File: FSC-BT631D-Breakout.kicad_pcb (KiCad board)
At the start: 2 copper layers, 46 parts, among them IC1 TLV320AIC3204IRHBR, J201 USB_C_Receptacle_USB2.0_16P, U202 AP63203WU-7

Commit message: power section done
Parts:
- added L201: 10uH, VLS5045EX-100M:VLS5045EX330M, F.Cu at (129.7, 59.2)
- added Q201: AONR21307, AONR21307:AONR21307, F.Cu at (128.6, 70.2)
- added U201: HUSB238_002DD, Package_DFN_QFN:DFN-10-1EP_3x3mm_P0.5mm_EP1.65x2.38mm_ThermalVias, F.Cu at (128.7, 65.6)
- moved C38 46.4 mm to (110.4, 56.4)
- moved C41 46.4 mm to (110.4, 63.9)
- moved C44 46.4 mm to (110.4, 68.9)
- moved C45 46.4 mm to (114.7, 56.4)
- moved R10 46.4 mm to (114.7, 68.9)
- moved R6 46.4 mm to (114.7, 63.9)
- moved C39 46.4 mm to (110.4, 58.9)
- moved C40 46.4 mm to (110.4, 61.4)
- moved C43 46.4 mm to (110.4, 66.4)
- moved C46 46.4 mm to (114.7, 58.9)
- moved R5 46.4 mm to (114.7, 61.4)
- moved R9 46.4 mm to (114.7, 66.4)
- moved R11 46.4 mm to (119.1, 56.4)
- moved R12 46.4 mm to (119.1, 58.9)
- moved R13 46.4 mm to (119.1, 61.4)
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
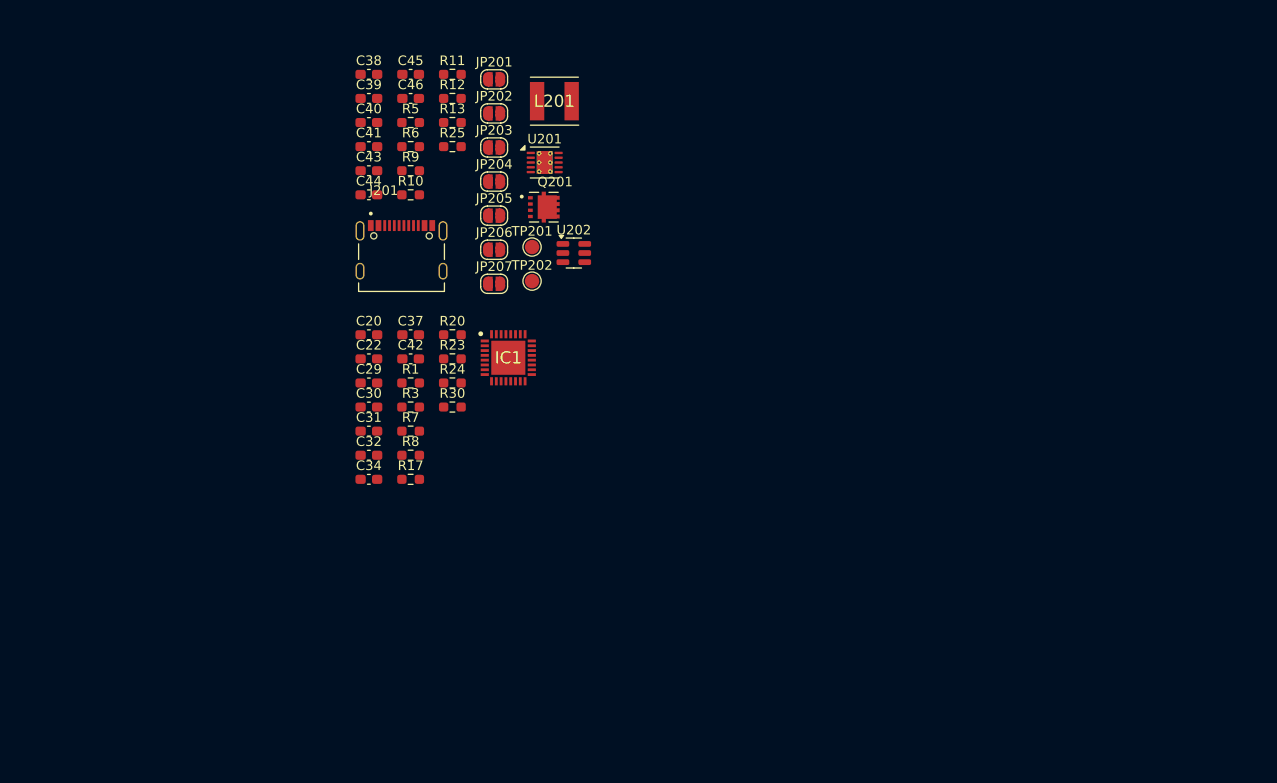
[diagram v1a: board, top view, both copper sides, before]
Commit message: schematic completed
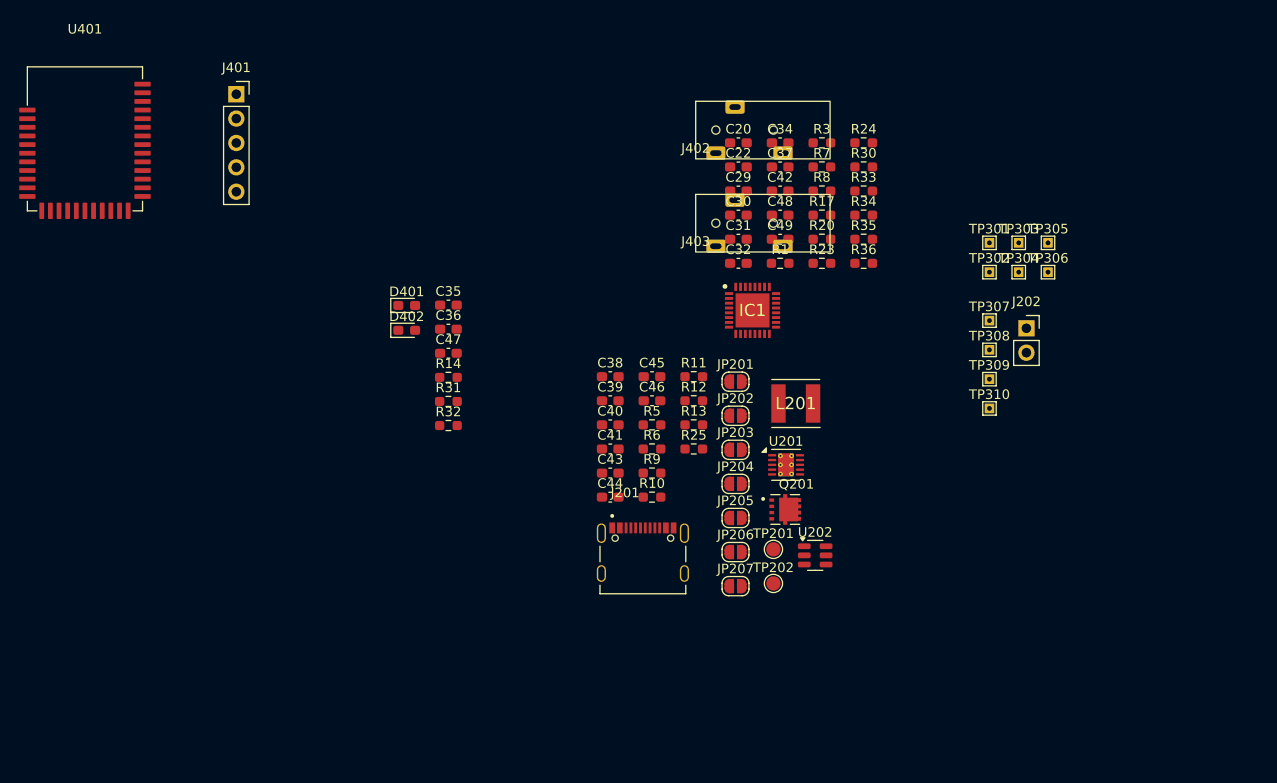
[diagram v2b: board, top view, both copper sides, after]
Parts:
- added C35: NC, Capacitor_SMD:C_0603_1608Metric_Pad1.08x0.95mm_HandSolder, F.Cu at (118.6, 80.4)
- added C36: NC, Capacitor_SMD:C_0603_1608Metric_Pad1.08x0.95mm_HandSolder, F.Cu at (118.6, 82.9)
- added C47: NC, Capacitor_SMD:C_0603_1608Metric_Pad1.08x0.95mm_HandSolder, F.Cu at (118.6, 85.4)
- added C48: 4.7uF, Capacitor_SMD:C_0603_1608Metric_Pad1.08x0.95mm_HandSolder, F.Cu at (153.2, 71.0)
- added C49: 4.7uF, Capacitor_SMD:C_0603_1608Metric_Pad1.08x0.95mm_HandSolder, F.Cu at (153.2, 73.6)
- added D401: LED2, LED_SMD:LED_0603_1608Metric_Pad1.05x0.95mm_HandSolder, F.Cu at (114.3, 80.5)
- added D402: LED1, LED_SMD:LED_0603_1608Metric_Pad1.05x0.95mm_HandSolder, F.Cu at (114.3, 83.0)
- added J202: J, Connector_PinSocket_2.54mm:PinSocket_1x02_P2.54mm_Vertical, F.Cu at (178.9, 82.8)
- added J401: UPDATE, Connector_PinSocket_2.54mm:PinSocket_1x05_P2.54mm_Vertical, F.Cu at (96.5, 58.5)
- added J402: LINE IN, XKB_PJ-3200:XKB_PJ-3200, F.Cu at (144.4, 64.6)
- added J403: LINE OUT, XKB_PJ-3200:XKB_PJ-3200, F.Cu at (144.4, 74.3)
- added R14: 0R, Resistor_SMD:R_0603_1608Metric_Pad0.98x0.95mm_HandSolder, F.Cu at (118.6, 87.9)
- added R31: 1K, Resistor_SMD:R_0603_1608Metric_Pad0.98x0.95mm_HandSolder, F.Cu at (118.6, 90.5)
- added R32: 1K, Resistor_SMD:R_0603_1608Metric_Pad0.98x0.95mm_HandSolder, F.Cu at (118.6, 93.0)
- added R33: 10K, Resistor_SMD:R_0603_1608Metric_Pad0.98x0.95mm_HandSolder, F.Cu at (161.9, 68.5)
- added R34: 10K, Resistor_SMD:R_0603_1608Metric_Pad0.98x0.95mm_HandSolder, F.Cu at (161.9, 71.0)
- added R35: 4.7K, Resistor_SMD:R_0603_1608Metric_Pad0.98x0.95mm_HandSolder, F.Cu at (161.9, 73.6)
- added R36: 4.7K, Resistor_SMD:R_0603_1608Metric_Pad0.98x0.95mm_HandSolder, F.Cu at (161.9, 76.1)
- added TP301: SCL, TestPoint:TestPoint_THTPad_1.0x1.0mm_Drill0.5mm, F.Cu at (175.0, 73.9)
- added TP302: SDA, TestPoint:TestPoint_THTPad_1.0x1.0mm_Drill0.5mm, F.Cu at (175.0, 77.0)
- added TP303: BLCK, TestPoint:TestPoint_THTPad_1.0x1.0mm_Drill0.5mm, F.Cu at (178.1, 73.9)
- added TP304: WS, TestPoint:TestPoint_THTPad_1.0x1.0mm_Drill0.5mm, F.Cu at (178.1, 77.0)
- added TP305: DOUT, TestPoint:TestPoint_THTPad_1.0x1.0mm_Drill0.5mm, F.Cu at (181.1, 73.9)
- added TP306: DIN, TestPoint:TestPoint_THTPad_1.0x1.0mm_Drill0.5mm, F.Cu at (181.1, 77.0)
- added TP307: VBUS, TestPoint:TestPoint_THTPad_1.0x1.0mm_Drill0.5mm, F.Cu at (175.0, 82.0)
- added TP308: VOUT, TestPoint:TestPoint_THTPad_1.0x1.0mm_Drill0.5mm, F.Cu at (175.0, 85.1)
- added TP309: 3.3V, TestPoint:TestPoint_THTPad_1.0x1.0mm_Drill0.5mm, F.Cu at (175.0, 88.1)
- added TP310: VDD, TestPoint:TestPoint_THTPad_1.0x1.0mm_Drill0.5mm, F.Cu at (175.0, 91.2)
- added U401: ~, FSC-BT631D:FSC-BT631D, F.Cu at (80.8, 63.1)
- moved C34 55.4 mm to (153.2, 63.5)
- moved R17 50.9 mm to (157.6, 71.0)
- moved R7 50.9 mm to (157.6, 66.0)
- moved R8 50.9 mm to (157.6, 68.5)
- moved R3 50.9 mm to (157.6, 63.5)
- moved R24 49.6 mm to (161.9, 63.5)
- moved R30 49.6 mm to (161.9, 66.0)
- moved C32 43.4 mm to (148.9, 76.1)
- moved C20 43.4 mm to (148.9, 63.5)
- moved C22 43.4 mm to (148.9, 66.0)
- moved C29 43.4 mm to (148.9, 68.5)
- moved C30 43.4 mm to (148.9, 71.0)
- moved C31 43.4 mm to (148.9, 73.6)
- moved C37 42.3 mm to (153.2, 66.0)
- moved C42 42.3 mm to (153.2, 68.5)
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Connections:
- net /power/VBUS renamed VBUS
- net Net-(IC1-AVDD) renamed /codec/AVDD

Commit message: FINALISED LAYOUT
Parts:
- removed C29, C30, C31: 10uF, Capacitor_SMD:C_0603_1608Metric_Pad1.08x0.95mm_HandSolder
- removed C32: 1uF, Capacitor_SMD:C_0603_1608Metric_Pad1.08x0.95mm_HandSolder
- removed C34: 220nF, Capacitor_SMD:C_0603_1608Metric_Pad1.08x0.95mm_HandSolder
- removed C35, C36, C47: NC, Capacitor_SMD:C_0603_1608Metric_Pad1.08x0.95mm_HandSolder
- removed C37, C39, C40, C41, C42, C43, C48, C49: 4.7uF, Capacitor_SMD:C_0603_1608Metric_Pad1.08x0.95mm_HandSolder
- removed C38: 1uF/50V, Capacitor_SMD:C_0603_1608Metric_Pad1.08x0.95mm_HandSolder
- removed C44: 0.1uF, Capacitor_SMD:C_0603_1608Metric_Pad1.08x0.95mm_HandSolder
- removed C45, C46: 22uF, Capacitor_SMD:C_0603_1608Metric_Pad1.08x0.95mm_HandSolder
- removed D401: LED2, LED_SMD:LED_0603_1608Metric_Pad1.05x0.95mm_HandSolder
- removed D402: LED1, LED_SMD:LED_0603_1608Metric_Pad1.05x0.95mm_HandSolder
- removed J201: USB_C_Receptacle_USB2.0_16P, SHOUHAN_TYPE-C_16PIN_2MD__073:SHOUHAN_TYPE-C_16PIN_2MD__073
- removed J202: J, Connector_PinSocket_2.54mm:PinSocket_1x02_P2.54mm_Vertical
- removed J401: UPDATE, Connector_PinSocket_2.54mm:PinSocket_1x05_P2.54mm_Vertical
- removed J402: LINE IN, XKB_PJ-3200:XKB_PJ-3200
- removed J403: LINE OUT, XKB_PJ-3200:XKB_PJ-3200
- removed JP201: 5V, Jumper:SolderJumper-2_P1.3mm_Open_RoundedPad1.0x1.5mm
- removed JP202: 9V, Jumper:SolderJumper-2_P1.3mm_Open_RoundedPad1.0x1.5mm
- removed JP203: 12V, Jumper:SolderJumper-2_P1.3mm_Open_RoundedPad1.0x1.5mm
- removed JP204: 15V, Jumper:SolderJumper-2_P1.3mm_Open_RoundedPad1.0x1.5mm
- removed JP205: 18V, Jumper:SolderJumper-2_P1.3mm_Open_RoundedPad1.0x1.5mm
- removed JP206: 1.25A, Jumper:SolderJumper-2_P1.3mm_Open_RoundedPad1.0x1.5mm
- removed JP207: 2.25A, Jumper:SolderJumper-2_P1.3mm_Open_RoundedPad1.0x1.5mm
- removed L201: 10uH, VLS5045EX-100M:VLS5045EX330M
- removed Q201: AONR21307, AONR21307:AONR21307
- removed R30, R35, R36: 4.7K, Resistor_SMD:R_0603_1608Metric_Pad0.98x0.95mm_HandSolder
- removed R31, R32: 1K, Resistor_SMD:R_0603_1608Metric_Pad0.98x0.95mm_HandSolder
- removed R33, R34: 10K, Resistor_SMD:R_0603_1608Metric_Pad0.98x0.95mm_HandSolder
- removed TP201: SCL, TestPoint:TestPoint_Pad_D1.5mm
- removed TP202: SDA, TestPoint:TestPoint_Pad_D1.5mm
- removed TP301: SCL, TestPoint:TestPoint_THTPad_1.0x1.0mm_Drill0.5mm
- removed TP302: SDA, TestPoint:TestPoint_THTPad_1.0x1.0mm_Drill0.5mm
- removed TP303: BLCK, TestPoint:TestPoint_THTPad_1.0x1.0mm_Drill0.5mm
- removed TP304: WS, TestPoint:TestPoint_THTPad_1.0x1.0mm_Drill0.5mm
- removed TP305: DOUT, TestPoint:TestPoint_THTPad_1.0x1.0mm_Drill0.5mm
- removed TP306: DIN, TestPoint:TestPoint_THTPad_1.0x1.0mm_Drill0.5mm
- removed TP307: VBUS, TestPoint:TestPoint_THTPad_1.0x1.0mm_Drill0.5mm
- removed TP308: VOUT, TestPoint:TestPoint_THTPad_1.0x1.0mm_Drill0.5mm
- removed TP309: 3.3V, TestPoint:TestPoint_THTPad_1.0x1.0mm_Drill0.5mm
- removed TP310: VDD, TestPoint:TestPoint_THTPad_1.0x1.0mm_Drill0.5mm
- removed U201: HUSB238_002DD, Package_DFN_QFN:DFN-10-1EP_3x3mm_P0.5mm_EP1.65x2.38mm_ThermalVias
- removed U202: AP63203WU-7, Package_TO_SOT_SMD:TSOT-23-6
- removed U401: ~, FSC-BT631D:FSC-BT631D
- added C1: 4.7uF, Capacitor_SMD:C_0603_1608Metric_Pad1.08x0.95mm_HandSolder, F.Cu at (116.8, 105.4)
- added C10: 10uF, Capacitor_SMD:C_0603_1608Metric_Pad1.08x0.95mm_HandSolder, F.Cu at (153.7, 100.3)
- added C11: 4.7uF, Capacitor_SMD:C_0603_1608Metric_Pad1.08x0.95mm_HandSolder, F.Cu at (153.7, 97.8)
- added C12: 1uF, Capacitor_SMD:C_0603_1608Metric_Pad1.08x0.95mm_HandSolder, F.Cu at (153.7, 102.9)
- added C13: 220nF, Capacitor_SMD:C_0603_1608Metric_Pad1.08x0.95mm_HandSolder, F.Cu at (153.7, 92.7)
- added C14: 100nF, Capacitor_SMD:C_0603_1608Metric_Pad1.08x0.95mm_HandSolder, F.Cu at (153.7, 105.4)
- added C15: 4.7uF, Capacitor_SMD:C_0603_1608Metric_Pad1.08x0.95mm_HandSolder, F.Cu at (149.9, 105.4)
- added C16: 4.7uF, Capacitor_SMD:C_0603_1608Metric_Pad1.08x0.95mm_HandSolder, F.Cu at (135.9, 105.4)
- added C17: 4.7uF, Capacitor_SMD:C_0603_1608Metric_Pad1.08x0.95mm_HandSolder, F.Cu at (141.0, 105.4)
- added C18: 10uF, Capacitor_SMD:C_0603_1608Metric_Pad1.08x0.95mm_HandSolder, F.Cu at (144.8, 105.4)
- added C19: 4.7uF, Capacitor_SMD:C_0603_1608Metric_Pad1.08x0.95mm_HandSolder, F.Cu at (147.3, 105.4)
- added C2: 4.7uF, Capacitor_SMD:C_0603_1608Metric_Pad1.08x0.95mm_HandSolder, F.Cu at (116.8, 102.9)
- added C21: NC, Capacitor_SMD:C_0603_1608Metric_Pad1.08x0.95mm_HandSolder, F.Cu at (130.7, 58.9)
- added C3: 4.7uF, Capacitor_SMD:C_0603_1608Metric_Pad1.08x0.95mm_HandSolder, F.Cu at (116.8, 100.3)
- added C4: 1uF/50V, Capacitor_SMD:C_0603_1608Metric_Pad1.08x0.95mm_HandSolder, F.Cu at (106.7, 110.5)
- added C5: 0.1uF, Capacitor_SMD:C_0603_1608Metric_Pad1.08x0.95mm_HandSolder, F.Cu at (104.1, 95.2)
- added C6: 4.7uF, Capacitor_SMD:C_0603_1608Metric_Pad1.08x0.95mm_HandSolder, F.Cu at (111.7, 96.5)
- added C7: 22uF, Capacitor_SMD:C_0603_1608Metric_Pad1.08x0.95mm_HandSolder, F.Cu at (113.0, 91.4)
- added C8: 22uF, Capacitor_SMD:C_0603_1608Metric_Pad1.08x0.95mm_HandSolder, F.Cu at (115.5, 91.4)
- added C9: 10uF, Capacitor_SMD:C_0603_1608Metric_Pad1.08x0.95mm_HandSolder, F.Cu at (153.7, 95.2)
- added D1: 3.3V, LED_SMD:LED_0603_1608Metric_Pad1.05x0.95mm_HandSolder, F.Cu at (100.3, 86.4)
- added D2: VDD, LED_SMD:LED_0603_1608Metric_Pad1.05x0.95mm_HandSolder, F.Cu at (115.5, 86.4)
- added D3: LED1, LED_SMD:LED_0603_1608Metric_Pad1.05x0.95mm_HandSolder, F.Cu at (120.0, 82.0)
- added D4: LED2, LED_SMD:LED_0603_1608Metric_Pad1.05x0.95mm_HandSolder, F.Cu at (124.5, 82.0)
- added J1: USB_C_Receptacle_USB2.0_16P, SHOUHAN_TYPE-C_16PIN_2MD__073:SHOUHAN_TYPE-C_16PIN_2MD__073, F.Cu at (104.1, 123.2)
- added J10: PIO, Connector_PinSocket_2.54mm:PinSocket_1x08_P2.54mm_Vertical, F.Cu at (94.0, 66.0)
- added J2: J, Connector_PinSocket_2.54mm:PinSocket_1x02_P2.54mm_Vertical, F.Cu at (106.7, 81.3)
- added J3: LINE IN, XKB_PJ-3200:XKB_PJ-3200, F.Cu at (140.8, 126.3)
- added J4: LINE OUT, XKB_PJ-3200:XKB_PJ-3200, F.Cu at (154.8, 126.3)
- added J5: USB_B_Micro, KH-MICRO5P-JN:KH-MICRO5P-JN, F.Cu at (157.5, 86.4)
- added J6: UPDATE, Connector_PinSocket_2.54mm:PinSocket_1x05_P2.54mm_Vertical, F.Cu at (160.0, 61.0)
- added J7: UART, Connector_PinSocket_2.54mm:PinSocket_1x06_P2.54mm_Vertical, F.Cu at (140.7, 55.9)
- added J8: I2C, Connector_PinSocket_2.54mm:PinSocket_1x04_P2.54mm_Vertical, F.Cu at (94.0, 88.9)
- added J9: NFC, Connector_PinSocket_2.54mm:PinSocket_1x02_P2.54mm_Vertical, F.Cu at (111.3, 75.7)
- added JP1: 5V, Jumper:SolderJumper-2_P1.3mm_Open_RoundedPad1.0x1.5mm, F.Cu at (99.0, 110.5)
- added JP2: 9V, Jumper:SolderJumper-2_P1.3mm_Open_RoundedPad1.0x1.5mm, F.Cu at (99.0, 108.0)
- added JP3: 12V, Jumper:SolderJumper-2_P1.3mm_Open_RoundedPad1.0x1.5mm, F.Cu at (99.0, 105.4)
- added JP4: 15V, Jumper:SolderJumper-2_P1.3mm_Open_RoundedPad1.0x1.5mm, F.Cu at (99.0, 102.9)
- added JP5: 1.25A, Jumper:SolderJumper-2_P1.3mm_Open_RoundedPad1.0x1.5mm, F.Cu at (119.4, 113.0)
- added JP6: 18V, Jumper:SolderJumper-2_P1.3mm_Open_RoundedPad1.0x1.5mm, F.Cu at (99.0, 100.3)
- added JP7: 2.25A, Jumper:SolderJumper-2_P1.3mm_Open_RoundedPad1.0x1.5mm, F.Cu at (119.4, 108.0)
- added JP8: LED1_S, Jumper:SolderJumper-2_P1.3mm_Bridged2Bar_RoundedPad1.0x1.5mm, F.Cu at (120.0, 75.7)
- added JP9: LED2_S, Jumper:SolderJumper-2_P1.3mm_Bridged2Bar_RoundedPad1.0x1.5mm, F.Cu at (124.5, 75.7)
- added L1: 10uH, VLS5045EX-100M:VLS5045EX330M, F.Cu at (107.9, 88.9)
- added Q1: AONR21307, AONR21307:AONR21307, F.Cu at (111.7, 105.4)
- added R15: 4.7K, Resistor_SMD:R_0603_1608Metric_Pad0.98x0.95mm_HandSolder, F.Cu at (135.9, 108.0)
- added R16: 0R, Resistor_SMD:R_0603_1608Metric_Pad0.98x0.95mm_HandSolder, F.Cu at (142.2, 92.7)
- added R18: 10K, Resistor_SMD:R_0603_1608Metric_Pad0.98x0.95mm_HandSolder, F.Cu at (141.0, 110.5)
- added R19: 4.7K, Resistor_SMD:R_0603_1608Metric_Pad0.98x0.95mm_HandSolder, F.Cu at (141.0, 108.0)
- added R2: 10R, Resistor_SMD:R_0603_1608Metric_Pad0.98x0.95mm_HandSolder, F.Cu at (106.7, 113.0)
- added R21: 4.7K, Resistor_SMD:R_0603_1608Metric_Pad0.98x0.95mm_HandSolder, F.Cu at (135.9, 97.8)
- added R22: 33R, Resistor_SMD:R_0603_1608Metric_Pad0.98x0.95mm_HandSolder, F.Cu at (135.9, 95.2)
- added R26: 0R, Resistor_SMD:R_0603_1608Metric_Pad0.98x0.95mm_HandSolder, F.Cu at (105.2, 65.0)
- added R27: 1K, Resistor_SMD:R_0603_1608Metric_Pad0.98x0.95mm_HandSolder, F.Cu at (120.0, 79.5)
- added R28: 1K, Resistor_SMD:R_0603_1608Metric_Pad0.98x0.95mm_HandSolder, F.Cu at (124.5, 79.5)
- added R4: 6K, Resistor_SMD:R_0603_1608Metric_Pad0.98x0.95mm_HandSolder, F.Cu at (104.1, 108.0)
- added TP1: VBUS, TestPoint:TestPoint_THTPad_1.0x1.0mm_Drill0.5mm, F.Cu at (99.0, 115.6)
- added TP10: LOR, TestPoint:TestPoint_THTPad_1.0x1.0mm_Drill0.5mm, F.Cu at (146.8, 115.3)
- added TP11: DIN, TestPoint:TestPoint_THTPad_1.0x1.0mm_Drill0.5mm, F.Cu at (139.7, 86.4)
- added TP12: LOL, TestPoint:TestPoint_THTPad_1.0x1.0mm_Drill0.5mm, F.Cu at (143.8, 115.3)
- added TP13: SCL, TestPoint:TestPoint_THTPad_1.0x1.0mm_Drill0.5mm, F.Cu at (129.5, 95.2)
- added TP14: SDA, TestPoint:TestPoint_THTPad_1.0x1.0mm_Drill0.5mm, F.Cu at (129.5, 100.3)
- added TP2: SCL, TestPoint:TestPoint_Pad_D1.5mm, F.Cu at (115.5, 115.6)
- added TP3: SDA, TestPoint:TestPoint_Pad_D1.5mm, F.Cu at (111.7, 115.6)
- added TP4: VOUT, TestPoint:TestPoint_THTPad_1.0x1.0mm_Drill0.5mm, F.Cu at (115.5, 96.5)
- added TP5: 3.3V, TestPoint:TestPoint_THTPad_1.0x1.0mm_Drill0.5mm, F.Cu at (102.8, 81.3)
- added TP6: VDD, TestPoint:TestPoint_THTPad_1.0x1.0mm_Drill0.5mm, F.Cu at (113.0, 81.3)
- added TP7: BLCK, TestPoint:TestPoint_THTPad_1.0x1.0mm_Drill0.5mm, F.Cu at (147.3, 86.4)
- added TP8: WS, TestPoint:TestPoint_THTPad_1.0x1.0mm_Drill0.5mm, F.Cu at (144.8, 86.4)
- added TP9: DOUT, TestPoint:TestPoint_THTPad_1.0x1.0mm_Drill0.5mm, F.Cu at (142.2, 86.4)
- added U1: HUSB238_002DD, Package_DFN_QFN:DFN-10-1EP_3x3mm_P0.5mm_EP1.65x2.38mm_ThermalVias, F.Cu at (111.7, 110.5)
- added U2: AP63203WU-7, Package_TO_SOT_SMD:TSOT-23-6, F.Cu at (107.9, 96.5)
- added U3: ~, FSC-BT631D:FSC-BT631D, F.Cu at (116.8, 61.0)
- C20: value 100nF -> NC
- C22: value 4.7uF -> NC
- R1: value 0R -> 49.9K
- R10: value 10K -> 1K
- R11: value 14K -> 220K
- R12: value 18K -> 0R
- R13: value 14K -> 0R
- R14: value 0R -> 10K
- R17: value 4.7K -> 0R
- R20: value 220K -> 4.7K
- R24: value 33R -> 22R
- R25: value 10R -> 22R
- R3: value 0R -> 5.1K
- R5: value 49.9K -> 10K
- R6: value 5.1K -> 14K
- R7: value 0R -> 18K
- R8: value 0R -> 14K
- R9: value 6K -> 1K
- moved R3 72.8 mm to (106.7, 115.6), turned to 180 degrees
- moved R1 64.6 mm to (102.1, 115.6), turned to 180 degrees
- moved R7 63.5 mm to (104.1, 100.3), turned to 180 degrees
- moved R8 56.7 mm to (119.4, 110.5), turned to 180 degrees
- moved R9 42.9 mm to (100.3, 81.3), turned to 90 degrees
- moved R5 37.9 mm to (104.1, 105.4), turned to 180 degrees
- moved R6 36.5 mm to (104.1, 102.9), turned to 180 degrees
- moved R20 36.4 mm to (135.9, 102.9)
- moved R23 32.5 mm to (135.9, 100.3)
- moved R10 30.9 mm to (115.5, 81.3), turned to 90 degrees
- moved R14 28.4 mm to (135.9, 110.5), turned to 180 degrees
- moved R17 28.1 mm to (139.7, 92.7), turned to -90 degrees
- moved R24 21.9 mm to (153.8, 83.9), turned to 90 degrees
- moved C20 19.5 mm to (130.7, 56.4)
- moved C22 18.7 mm to (130.7, 61.5)
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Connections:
- C20 pad 1: +3V3 -> Net-(U3-RF)
- C20 pad 2: GND -> Net-(AE1-A)
- C22 pad 1: /codec/AVDD -> GND
- C22 pad 2: GND -> Net-(AE1-A)
- IC1 pad 15: L_LIN2 -> L_LINE2
- IC1 pad 22: unconnected-(IC1-LOL-Pad22) -> Net-(IC1-LOL)
- IC1 pad 23: unconnected-(IC1-LOR-Pad23) -> Net-(IC1-LOR)
- IC1 pad 26: +3V3 -> +3.3V
- IC1 pad 30: +3V3 -> +3.3V
- IC1 pad 6: +3V3 -> +3.3V
- R1 pad 1: P0.15/I2S_DOUT -> Net-(Q1-Pad4)
- R1 pad 2: /codec/I2S2_DO -> VBUS
- R10 pad 1: /power/VSET -> Net-(D2-A)
- R10 pad 2: Net-(JP203-A) -> VDD
- R11 pad 1: /power/VSET -> Net-(IC1-~{RESET})
- R11 pad 2: Net-(JP204-A) -> +3.3V
- R12 pad 1: /power/VSET -> P0.14/I2S_BCLK
- R12 pad 2: Net-(JP205-A) -> /codec/I2S2_CLK
- R13 pad 1: /power/ISET -> P0.16/I2S_WS
- R13 pad 2: Net-(JP207-A) -> /codec/I2S2_WS
- R14 pad 1: VDD -> Net-(C16-Pad1)
- R17 pad 1: +3V3 -> P0.13/I2S_DIN
- R17 pad 2: Net-(IC1-SCL/~{SS}) -> /codec/I2S2_DI
- R20 pad 1: Net-(IC1-~{RESET}) -> +3.3V
- R20 pad 2: +3V3 -> Net-(IC1-SDA/MOSI)
- R23 pad 1: P1.03/I2C_SCL -> P1.02/I2C_SDA
- R23 pad 2: Net-(IC1-SCL/~{SS}) -> Net-(IC1-SDA/MOSI)
- R24 pad 1: P1.02/I2C_SDA -> /module/MOD_D+
- R24 pad 2: Net-(IC1-SDA/MOSI) -> /module/USB_D+
- R25 pad 1: Net-(U201-VIN) -> /module/MOD_D-
- R25 pad 2: VBUS -> /module/USB_D-
- R3 pad 1: P0.14/I2S_BCLK -> Net-(U1-GATE)
- R3 pad 2: /codec/I2S2_CLK -> Net-(Q1-Pad4)
- R5 pad 1: Net-(Q201-Pad4) -> /power/VSET
- R5 pad 2: VBUS -> Net-(JP3-A)
- R6 pad 1: Net-(U201-GATE) -> /power/VSET
- R6 pad 2: Net-(Q201-Pad4) -> Net-(JP4-A)
- R7 pad 1: P0.13/I2S_DIN -> /power/VSET
- R7 pad 2: /codec/I2S2_DI -> Net-(JP6-A)
- R8 pad 1: P0.16/I2S_WS -> /power/ISET
- R8 pad 2: /codec/I2S2_WS -> Net-(JP7-A)
- R9 pad 1: /power/VSET -> Net-(D1-A)
- R9 pad 2: Net-(JP202-A) -> +3.3V
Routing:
- net VDD: track 0.00 -> 110.7 mm, vias 0 -> 2
- net P1.02/I2C_SDA: track 0.00 -> 82.3 mm, vias 0 -> 2
- net +3.3V: track 0.00 -> 82.1 mm, vias 0 -> 11
- net P1.03/I2C_SCL: track 0.00 -> 77.2 mm, vias 0 -> 2
- net P0.14/I2S_BCLK: track 0.00 -> 52.7 mm
- net P0.16/I2S_WS: track 0.00 -> 49.3 mm, vias 0 -> 1
- net P0.15/I2S_DOUT: track 0.00 -> 48.4 mm
- net P0.13/I2S_DIN: track 0.00 -> 44.6 mm, vias 0 -> 1
- net +5V: track 0.00 -> 43.8 mm, vias 0 -> 2
- net SWDIO: track 0.00 -> 39.8 mm
- net /module/USB_D-: track 0.00 -> 39.4 mm, vias 0 -> 2
- net /module/USB_D+: track 0.00 -> 39.2 mm
- net SWDCLK: track 0.00 -> 38.7 mm
- net P1.1/UART_RTS: track 0.00 -> 38.4 mm
- net RESET: track 0.00 -> 37.9 mm, vias 0 -> 2
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- added copper zone on F.Cu, net +3.3V
- added copper zone on F.Cu, net /power/SW
- added copper zone on F.Cu, net /power/VOUT
- added copper zone on B.Cu, net GND
- added copper zone on F.Cu, net GND
- added copper zone on F.Cu, net VBUS
- added copper zone on F.Cu, net VDD
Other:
- board outline added: 70.6 x 72.9 mm
- board text added: "00"
- board text added: "01"
- board text added: "06"
- board text added: "07"
- board text added: "1.25A"
- board text added: "12V"
- board text added: "15V"
- board text added: "18V"
- board text added: "2.25A"
- board text added: "22"
- board text added: "23"
- board text added: "24"
- board text added: "25"
- board text added: "26"
- board text added: "27"
- board text added: "3.3V"
- board text added: "5V"
- board text added: "9V"
- board text added: "BLCK"
- board text added: "CTS"
- board text added: "DIN"
- board text added: "DOUT"
- board text added: "ENABLE MODULE"
- board text added: "GND"
- board text added: "HPL"
- board text added: "HPR"
- board text added: "LOL"
- board text added: "LOR"
- board text added: "L_LINE"
- board text added: "NFC1"
- board text added: "NFC2"
- board text added: "RESET"
- board text added: "RTS"
- board text added: "RXD"
- board text added: "R_LINE"
- board text added: "SCL"
- board text added: "SDA"
- board text added: "SWCLK"
- board text added: "SWDIO"
- board text added: "TXD"
- board text added: "VBUS"
- board text added: "VDD"
- board text added: "VOUT"
- board text added: "WS"

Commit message: fixed silkscreen
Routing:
- net GND: vias 71 -> 76
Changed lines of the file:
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@@
 		(tags "resistor handsolder")
 		(property "Reference" "R5"
-			(at -3.322 0 0)
+			(at -3.068 0 0)
 			(layer "F.SilkS")
 			(effects
@@
 	)
 	(segment
+		(start 147.447 99.187)
+		(end 147.32 99.06)
+		(width 0.2)
+		(layer "F.Cu")
+		(net 1)
+	)
+	(segment
+		(start 146.07 97.79)
+		(end 146.07 97.81)
+		(width 0.2)
+		(layer "F.Cu")
+		(net 1)
+	)
+	(segment
 		(start 147.32 99.06)
 		(end 147.07 98.81)
@@
 	)
 	(segment
+		(start 146.05 100.33)
+		(end 147.32 99.06)
+		(width 0.2)
+		(layer "F.Cu")
+		(net 1)
+	)
+	(segment
 		(start 149.77 99.31)
 		(end 147.57 99.31)
@@
 	(segment
 		(start 145.596 100.784)
-		(end 147.32 99.06)
+		(end 146.05 100.33)
 		(width 0.2)
 		(layer "F.Cu")
@@
 	)
 	(segment
+		(start 146.05 98.81)
+		(end 144.87 98.81)
+		(width 0.2)
+		(layer "F.Cu")
+		(net 1)
+	)
+	(segment
+		(start 146.812 98.81)
+		(end 146.05 98.81)
+		(width 0.2)
+		(layer "F.Cu")
+		(net 1)
+	)
+	(segment
 		(start 107.32 118.46)
 		(end 107.67 118.11)
@@
 	(segment
 		(start 147.57 99.31)
-		(end 147.32 99.06)
+		(end 147.447 99.187)
 		(width 0.2)
 		(layer "F.Cu")
@@
 	(segment
 		(start 146.07 96.61)
-		(end 146.07 97.81)
+		(end 146.07 97.79)
 		(width 0.2)
 		(layer "F.Cu")
@@
 	(segment
 		(start 147.07 98.81)
-		(end 144.87 98.81)
+		(end 146.812 98.81)
 		(width 0.2)
 		(layer "F.Cu")
@@
 	)
 	(via
+		(at 147.447 99.187)
+		(size 0.6)
+		(drill 0.3)
+		(layers "F.Cu" "B.Cu")
+		(net 1)
+	)
+	(via
 		(at 124.46 57.404)
 		(size 0.6)
@@
 	)
 	(via
+		(at 146.05 100.33)
+		(size 0.6)
+		(drill 0.3)
+		(layers "F.Cu" "B.Cu")
+		(net 1)
+	)
+	(via
 		(at 110.47 93.98)
 		(size 0.6)
@@
 	)
 	(via
+		(at 146.812 98.81)
+		(size 0.6)
+		(drill 0.3)
+		(layers "F.Cu" "B.Cu")
+		(net 1)
+	)
+	(via
+		(at 146.05 98.81)
+		(size 0.6)
+		(drill 0.3)
+		(layers "F.Cu" "B.Cu")
+		(net 1)
+	)
+	(via
 		(at 121.392 107.95)
 		(size 0.6)
@@
 		(size 0.6)
 		(drill 0.3)
+		(layers "F.Cu" "B.Cu")
+		(net 1)
+	)
+	(via
+		(at 146.07 97.79)
+		(size 0.6)
+		(drill 0.3)

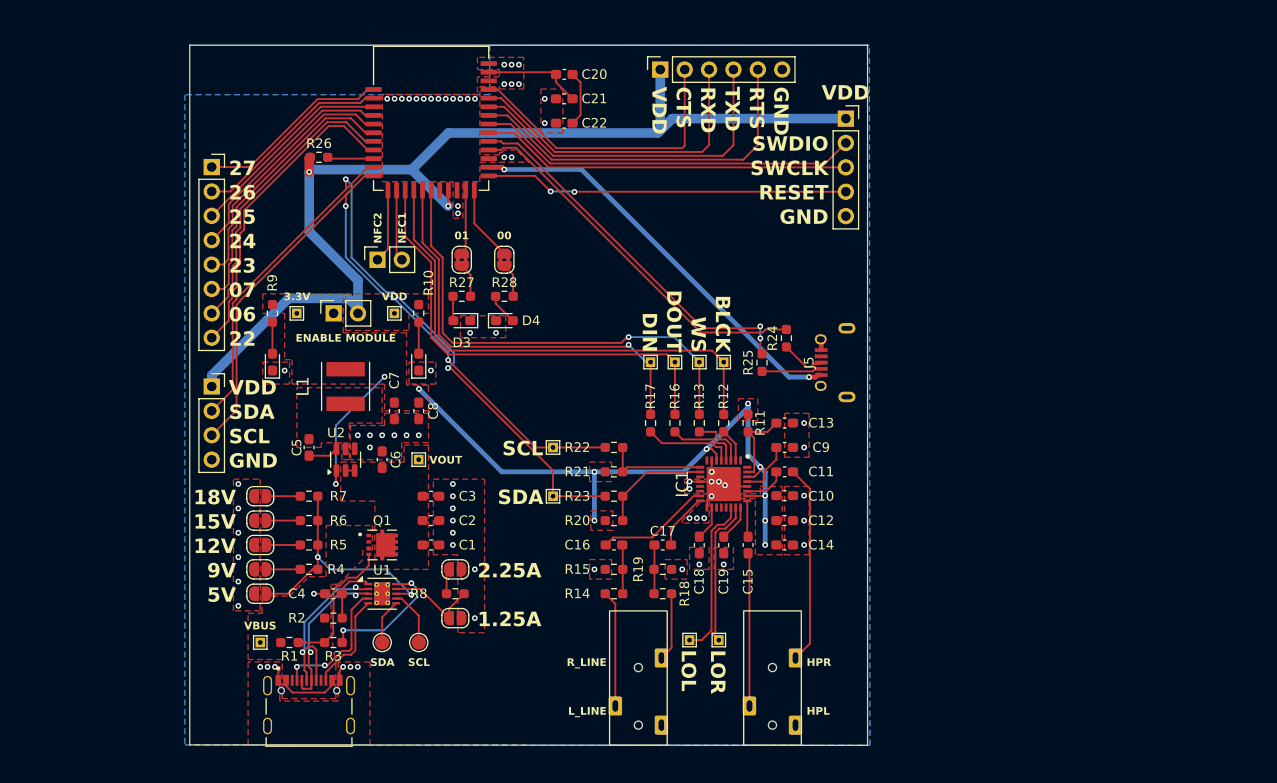
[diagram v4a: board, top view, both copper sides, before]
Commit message: fixed ground pour
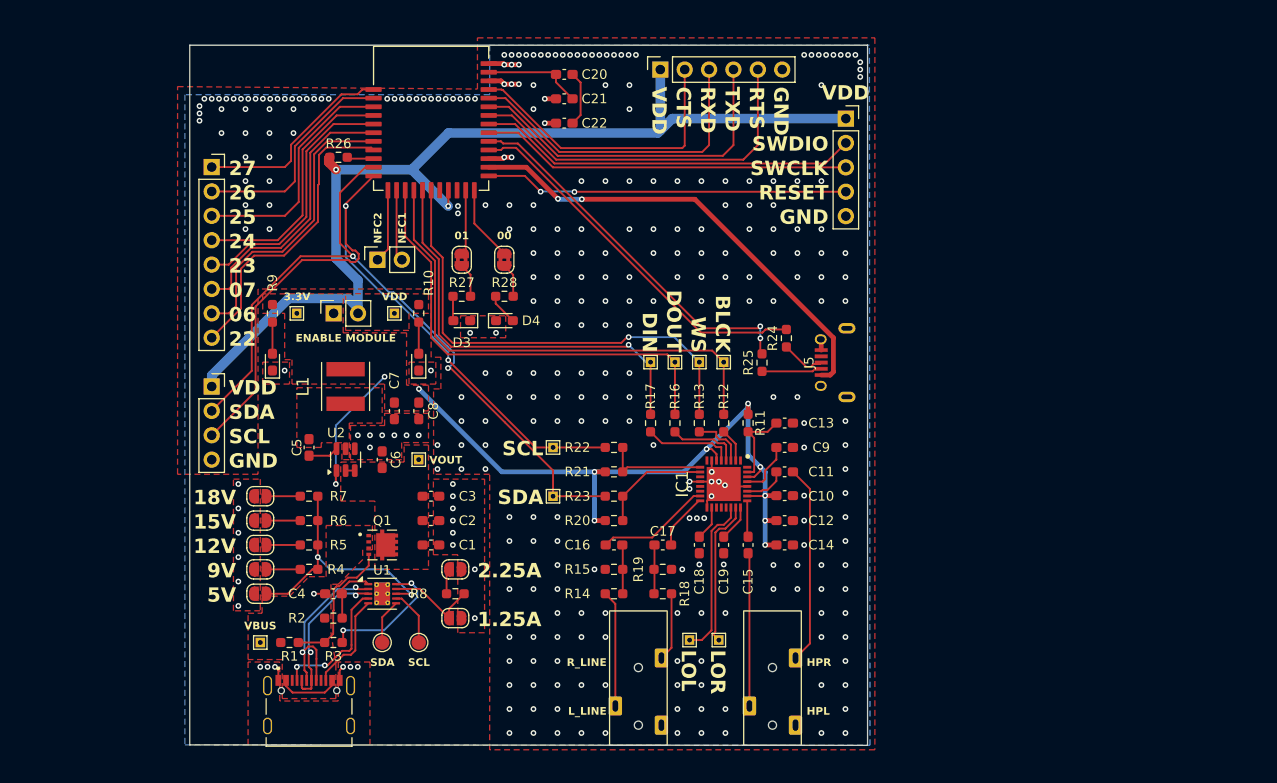
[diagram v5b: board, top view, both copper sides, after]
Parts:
- moved R26 2.03 mm to (107.2, 65.0)
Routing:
- net GND: track 17.8 -> 29.0 mm, vias 76 -> 318
- net +3.3V: track 82.1 -> 89.0 mm
- net P1.02/I2C_SDA: track 82.3 -> 77.2 mm
- net +5V: track 43.8 -> 48.2 mm
- net VDD: track 110.7 -> 107.1 mm
- net P0.25: track 21.6 -> 24.9 mm
- net P1.03/I2C_SCL: track 77.2 -> 79.8 mm
- net P0.24: track 23.8 -> 26.3 mm
- net P0.26: track 20.9 -> 23.0 mm
- net Net-(U3-NC): track 4.83 -> 2.80 mm
- net P0.22: track 32.8 -> 31.6 mm
- net P0.27: track 20.2 -> 21.2 mm

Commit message: added ibom & fabrication files
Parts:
- added AE1: Antenna_Shield, Connector_Coaxial:U.FL_Hirose_U.FL-R-SMT-1_Vertical, F.Cu at (135.8, 57.4)
- J2: value J -> M_EN
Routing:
- net Net-(AE1-A): track 5.77 -> 10.0 mm
- net +5V: track 48.2 -> 48.8 mm
- net GND: vias 318 -> 322
